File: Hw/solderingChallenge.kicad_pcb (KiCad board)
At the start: 2 copper layers, 33.5 x 33.5 mm, 28 parts, among them J2 SWD, SW1 SW_RST, SW2 On, U1 PY32F002AA15M6TU

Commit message: feat: add labels
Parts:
- added kibuzzard-67916211: G***, kibuzzard-67916211, B.Cu at (156.9, 79.5)
- added kibuzzard-6791629E: G***, kibuzzard-6791629E, B.Cu at (156.9, 79.5)
- added kibuzzard-6797B453: G***, kibuzzard-6797B453, B.Cu at (142.2, 76.2)
- moved kibuzzard-679168C7 1.01 mm to (155.1, 78.3), turned to 90 degrees

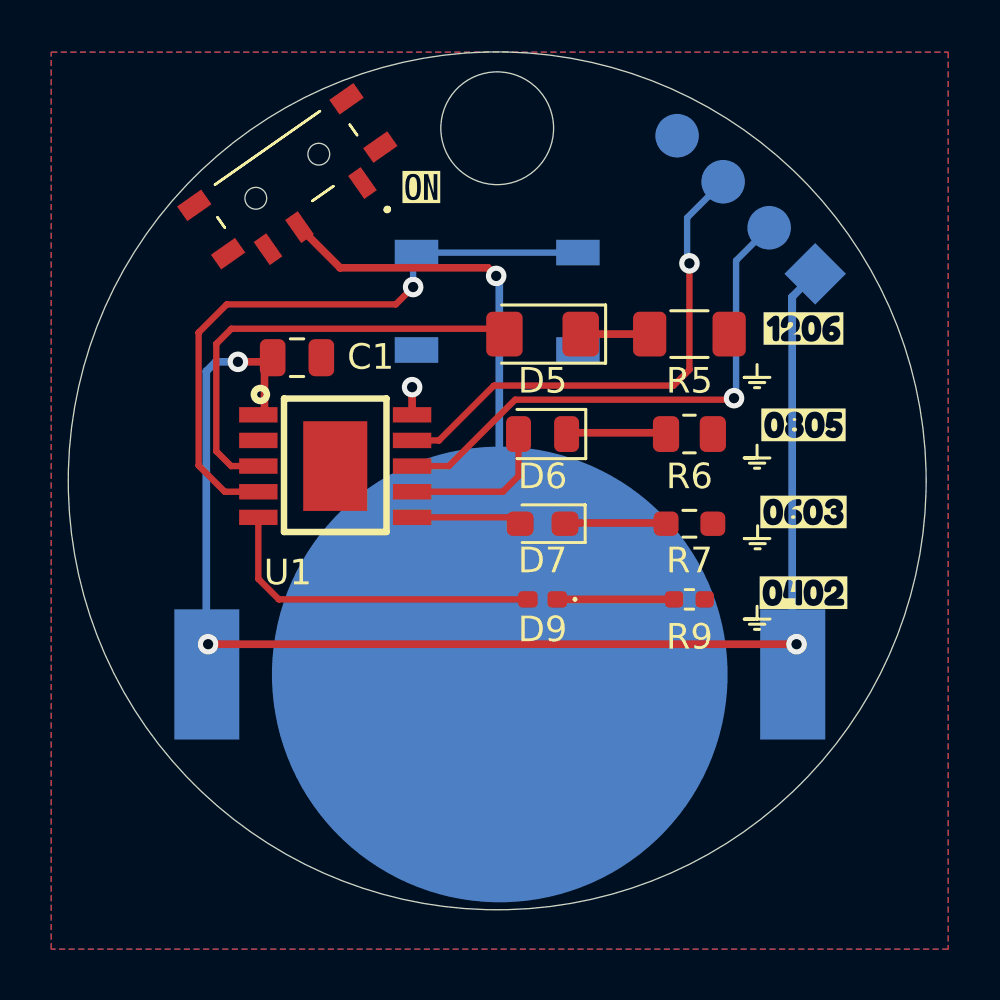
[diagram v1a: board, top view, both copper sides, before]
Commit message: fix(Hw): Update Logo and tags
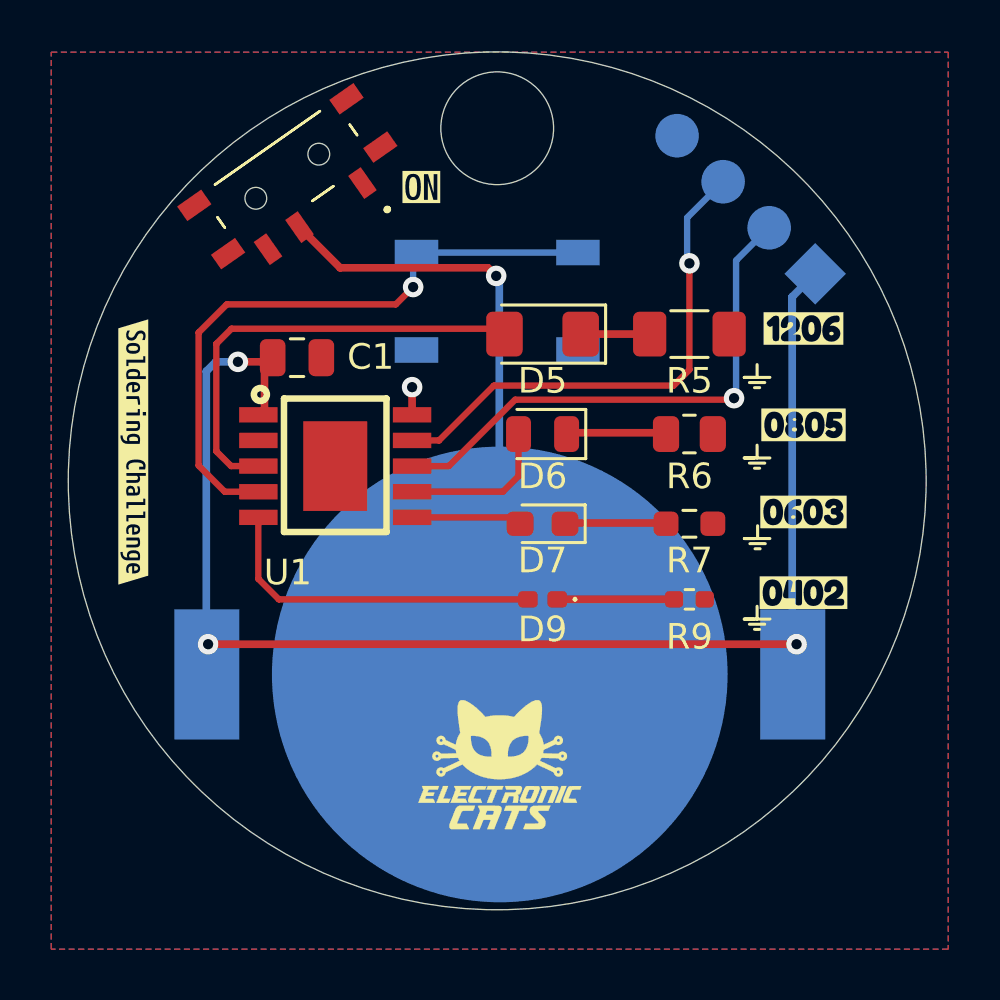
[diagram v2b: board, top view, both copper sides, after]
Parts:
- removed the G*** at (142.4, 88.5)
- removed kibuzzard-67916211 (x2): G***, kibuzzard-67916211
- removed kibuzzard-6791629E (x2): G***, kibuzzard-6791629E
- added kibuzzard-67996501: G***, kibuzzard-67996501, F.Cu at (128.2, 78.1)
- added kibuzzard-67996501: G***, kibuzzard-67996501, B.Cu at (157.1, 78.9)
- moved G*** 2.26 mm to (142.5, 90.3)
